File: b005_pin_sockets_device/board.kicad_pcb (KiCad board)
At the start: 4 copper layers, 21 x 13 mm, 6 parts, among them J1 Conn_01x10_Male, J2 Conn_01x05_Male, J3 Conn_01x05_Male, J4 Conn_01x05_Male, J5 Conn_01x05_Male, J6 Conn_01x10_Male

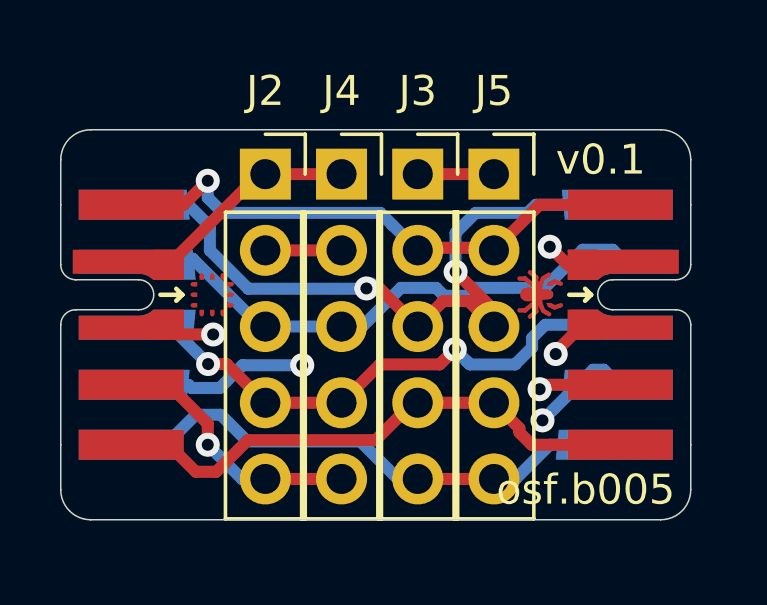
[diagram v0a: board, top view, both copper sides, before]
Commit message: changed name to 144pin tqfp because many chips are compatible with the board
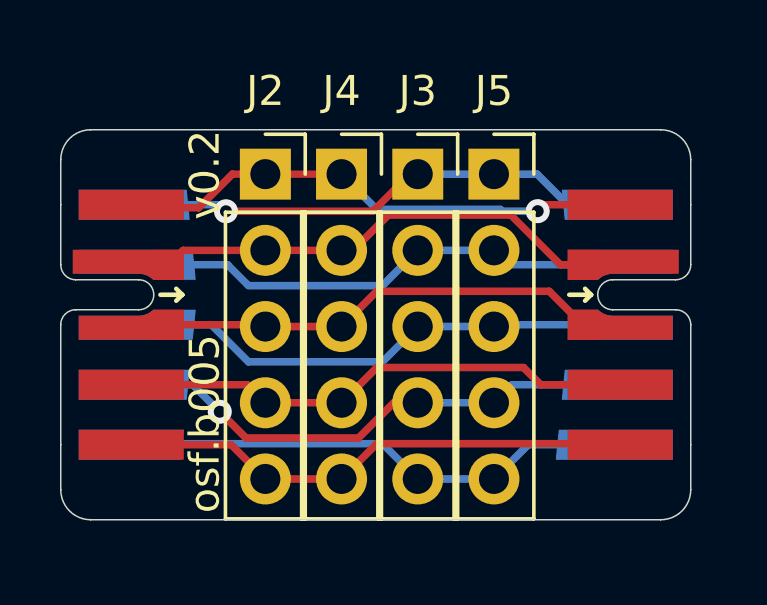
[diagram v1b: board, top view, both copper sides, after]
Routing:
- net Net-(J1-Pad6): track 31.8 -> 17.2 mm, vias 2 -> 1
- net Net-(J1-Pad8): track 24.9 -> 17.8 mm, vias 2 -> 0
- net Net-(J1-Pad3): track 21.3 -> 14.8 mm
- net Net-(J1-Pad2): track 18.9 -> 15.2 mm, vias 2 -> 0
- net Net-(J1-Pad5): track 20.7 -> 17.3 mm, vias 2 -> 0
- net Net-(J1-Pad4): track 19.6 -> 17.3 mm, vias 2 -> 0
- net Net-(J1-Pad10): track 18.6 -> 17.2 mm
- net Net-(J1-Pad7): track 18.6 -> 17.8 mm, vias 1 -> 0
- net Net-(J1-Pad1): track 18.1 -> 17.4 mm
- net Net-(J1-Pad9): track 18.3 -> 17.7 mm, vias 0 -> 1
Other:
- board text added: "v0.2"
- board text removed: "v0.1"
